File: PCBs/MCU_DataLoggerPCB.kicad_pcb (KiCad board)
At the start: 2 copper layers, 53.8 x 36.1 mm, 30 parts, among them J1 Conn_01x04_Pin, J2 Conn_01x04_Pin, J3 Conn_01x09_Pin, J4 Conn_02x03_Odd_Even, U1 24LC1025, U2 24LC1025, U3 DS1337S+, U4 ATMEGA328P-AU, Y1 32.768 kHz, Y2 16 MHz

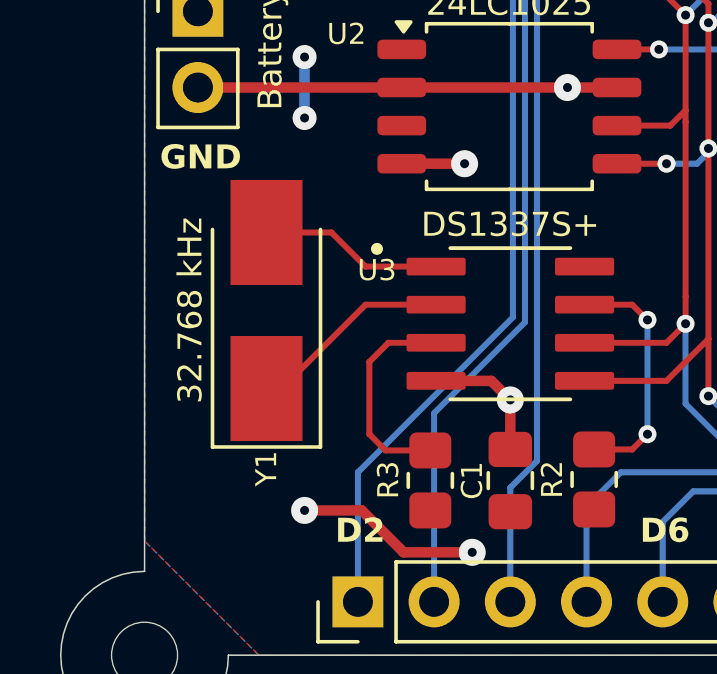
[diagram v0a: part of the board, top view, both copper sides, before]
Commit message: Project: Added BOM and changed 32.768kHz crystal footprint to match element that was available to buy at the moment
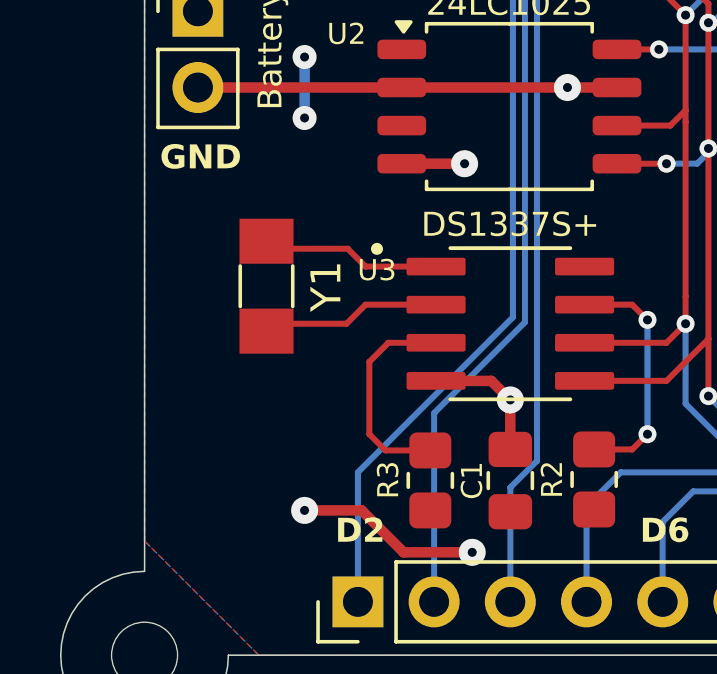
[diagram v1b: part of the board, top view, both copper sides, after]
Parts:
- Y1: footprint Crystal:Crystal_SMD_5032-2Pin_5.0x3.2mm_HandSoldering -> Crystal:Crystal_SMD_3215-2Pin_3.2x1.5mm
- moved Y1 0.81 mm to (49.8, 89.8), turned to -90 degrees
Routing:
- net Net-(U3-X2): track 6.81 -> 5.92 mm
